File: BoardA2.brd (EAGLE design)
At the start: 44 x 93 mm, 18 parts, among them J1 FEMALE 2x3, T1 2N2222

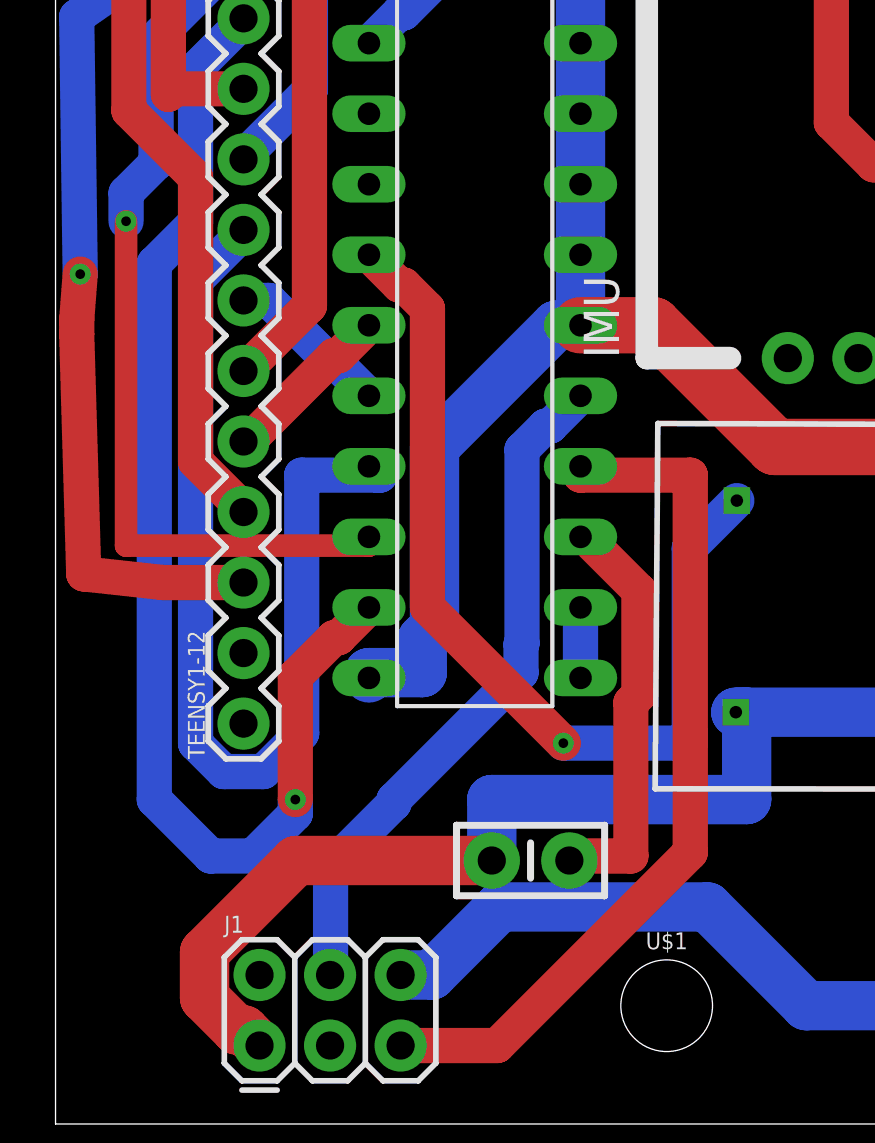
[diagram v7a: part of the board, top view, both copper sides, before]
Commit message: wire missing connection
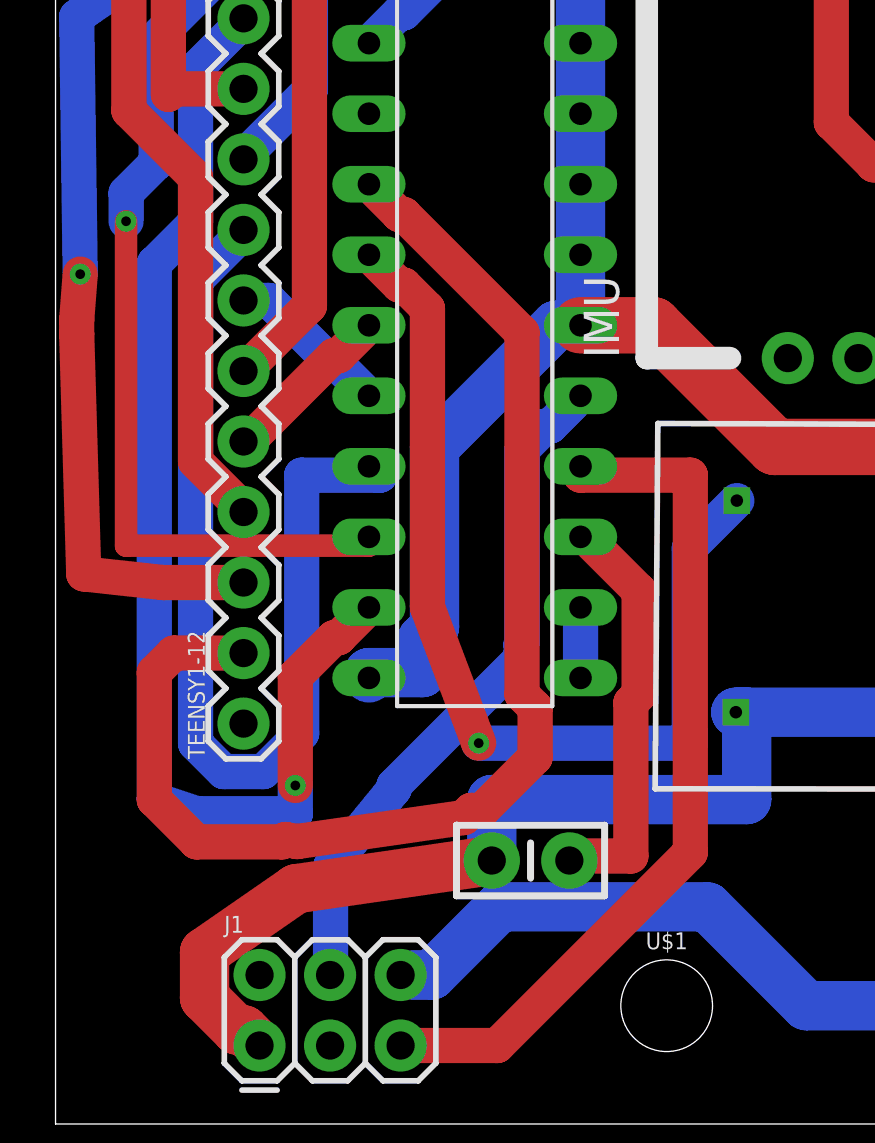
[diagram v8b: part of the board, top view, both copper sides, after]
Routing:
- net ADC-CON: track 0.00 -> 46.6 mm
- net ADC-DIN: track 44.6 -> 43.3 mm
- net N$4: track 34.6 -> 36.0 mm
- net GND: track 180.3 -> 179.7 mm
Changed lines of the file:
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@@
 <wire x1="7.3472" y1="2.826" x2="6.7884" y2="3.3848" width="1.778" layer="1"/>
 <wire x1="6.7884" y1="3.3848" x2="6.52655625" y2="3.3848" width="1.778" layer="1"/>
-<wire x1="8.66835625" y1="9.489" x2="15.711" y2="9.489" width="1.778" layer="1"/>
-<wire x1="5.366" y1="6.18664375" x2="8.66835625" y2="9.489" width="1.778" layer="1"/>
+<wire x1="8.66835625" y1="8.473" x2="15.711" y2="9.489" width="1.778" layer="1"/>
+<wire x1="5.366" y1="6.18664375" x2="8.66835625" y2="8.473" width="1.778" layer="1"/>
 <wire x1="15.711" y1="9.489" x2="15.711" y2="11.684" width="1.778" layer="16"/>
 <wire x1="15.711" y1="11.684" x2="24.892" y2="11.684" width="1.778" layer="16"/>
@@
 <wire x1="12.3792" y1="30.2128" x2="12.5471" y2="30.2128" width="1.27" layer="1"/>
 <wire x1="13.3952" y1="29.3647" x2="13.3952" y2="18.6088" width="1.27" layer="1"/>
-<wire x1="13.3952" y1="18.6088" x2="18.288" y2="13.716" width="1.27" layer="1"/>
-<via x="18.288" y="13.716" extent="1-16" drill="0.35"/>
-<wire x1="18.288" y1="13.716" x2="22.86" y2="13.716" width="1.27" layer="16"/>
+<wire x1="13.3952" y1="18.6088" x2="15.24" y2="13.716" width="1.27" layer="1"/>
+<via x="15.24" y="13.716" extent="1-16" drill="0.35"/>
+<wire x1="15.24" y1="13.716" x2="22.86" y2="13.716" width="1.27" layer="16"/>
 <wire x1="22.86" y1="13.716" x2="22.86" y2="14.100575" width="1.27" layer="16"/>
 <wire x1="22.86" y1="14.100575" x2="22.82434375" y2="14.13623125" width="1.27" layer="16"/>
@@
 <wire x1="5.0428" y1="37.99543125" x2="5.0428" y2="32.4748" width="1.27" layer="16"/>
 <wire x1="3.556" y1="30.988" x2="3.556" y2="11.684" width="1.27" layer="16"/>
-<wire x1="3.556" y1="11.684" x2="5.588" y2="9.652" width="1.27" layer="16"/>
-<wire x1="5.588" y1="9.652" x2="7.112" y2="9.652" width="1.27" layer="16"/>
-<wire x1="8.636" y1="11.176" x2="7.112" y2="9.652" width="1.27" layer="16"/>
-<via x="8.636" y="11.684" extent="1-16" drill="0.35"/>
-<wire x1="8.636" y1="11.176" x2="8.636" y2="11.684" width="1.27" layer="16"/>
+<wire x1="3.556" y1="11.684" x2="5.08" y2="11.176" width="1.27" layer="16"/>
+<wire x1="5.08" y1="11.176" x2="8.636" y2="11.176" width="1.27" layer="16"/>
+<via x="8.636" y="12.192" extent="1-16" drill="0.35"/>
+<wire x1="8.636" y1="11.176" x2="8.636" y2="12.192" width="1.27" layer="16"/>
 <wire x1="10.0269" y1="17.5128" x2="10.1948" y2="17.5128" width="1.27" layer="1"/>
 <wire x1="10.1948" y1="17.5128" x2="11.287" y2="18.605" width="1.27" layer="1"/>
-<wire x1="8.636" y1="11.684" x2="8.636" y2="16.1219" width="1.27" layer="1"/>
+<wire x1="8.636" y1="12.192" x2="8.636" y2="16.1219" width="1.27" layer="1"/>
 <wire x1="8.636" y1="16.1219" x2="10.0269" y2="17.5128" width="1.27" layer="1"/>
 </signal>
@@
 <wire x1="17.8148" y1="25.1328" x2="18.907" y2="26.225" width="1.27" layer="16"/>
 <wire x1="16.7988" y1="17.3068" x2="16.764" y2="17.272" width="1.27" layer="16"/>
-<wire x1="16.764" y1="17.272" x2="16.764" y2="16.256" width="1.27" layer="16"/>
-<wire x1="12.192" y1="11.684" x2="12.192" y2="11.557" width="1.27" layer="16"/>
-<wire x1="12.192" y1="11.557" x2="9.906" y2="9.271" width="1.27" layer="16"/>
+<wire x1="16.764" y1="17.272" x2="16.764" y2="16.764" width="1.27" layer="16"/>
+<wire x1="12.192" y1="12.192" x2="12.192" y2="12.065" width="1.27" layer="16"/>
+<wire x1="12.192" y1="12.065" x2="9.906" y2="9.271" width="1.27" layer="16"/>
 <wire x1="9.906" y1="9.271" x2="9.906" y2="5.3848" width="1.27" layer="16"/>
 <wire x1="9.906" y1="5.3848" x2="9.8872" y2="5.366" width="1.27" layer="16"/>
 <wire x1="16.7988" y1="24.2847" x2="16.7988" y2="17.3068" width="1.27" layer="16"/>
-<wire x1="16.764" y1="16.256" x2="12.192" y2="11.684" width="1.27" layer="16"/>
+<wire x1="16.764" y1="16.764" x2="12.192" y2="12.192" width="1.27" layer="16"/>
 </signal>
 <signal name="E+">
@@
 <contactref element="ADC" pad="5"/>
 <contactref element="TEENSY1-12" pad="2"/>
-<wire x1="6.77" y1="16.96" x2="11.287" y2="33.845" width="0" layer="19" extent="1-1"/>
+<wire x1="6.77" y1="16.96" x2="4.26" y2="16.96" width="1.27" layer="1"/>
+<wire x1="4.26" y1="16.96" x2="3.556" y2="16.256" width="1.27" layer="1"/>
+<wire x1="3.556" y1="16.256" x2="3.556" y2="11.684" width="1.27" layer="1"/>
+<wire x1="3.556" y1="11.684" x2="5.08" y2="10.16" width="1.27" layer="1"/>
+<wire x1="5.08" y1="10.16" x2="8.159975" y2="10.16" width="1.27" layer="1"/>
+<wire x1="8.159975" y1="10.16" x2="8.28501875" y2="10.246571875" width="1.27" layer="1"/>
+<wire x1="8.28501875" y1="10.246571875" x2="8.6994125" y2="10.1712375" width="1.27" layer="1"/>
+<wire x1="8.6994125" y1="10.1712375" x2="14.709946875" y2="11.038340625" width="1.27" layer="1"/>
+<wire x1="14.709946875" y1="11.038340625" x2="14.96400625" y2="11.2924" width="1.27" layer="1"/>
+<wire x1="14.96400625" y1="11.2924" x2="15.3564" y2="11.2924" width="1.27" layer="1"/>
+<wire x1="15.3564" y1="11.2924" x2="17.272" y2="13.208" width="1.27" layer="1"/>
+<wire x1="17.272" y1="13.208" x2="17.272" y2="14.9921" width="1.27" layer="1"/>
+<wire x1="17.272" y1="14.9921" x2="16.7988" y2="15.4653" width="1.27" layer="1"/>
+<wire x1="12.5471" y1="32.7528" x2="12.3792" y2="32.7528" width="1.27" layer="1"/>
+<wire x1="12.3792" y1="32.7528" x2="11.287" y2="33.845" width="1.27" layer="1"/>
+<wire x1="16.7988" y1="15.4653" x2="16.7988" y2="28.5011" width="1.27" layer="1"/>
+<wire x1="16.7988" y1="28.5011" x2="12.5471" y2="32.7528" width="1.27" layer="1"/>
 </signal>
 </signals>
